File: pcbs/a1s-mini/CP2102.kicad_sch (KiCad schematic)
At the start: 12 parts, among them U3 CP2102N

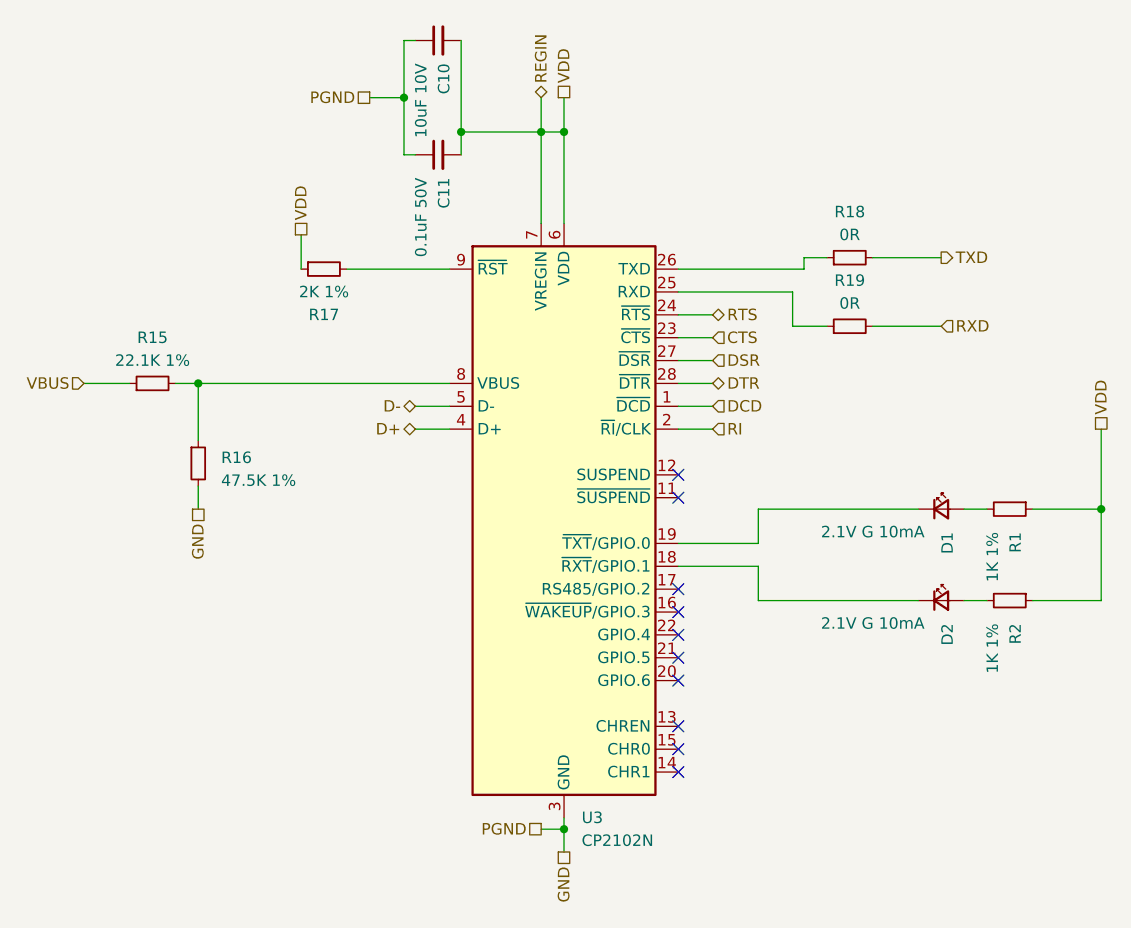
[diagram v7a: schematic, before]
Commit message: Collateral update of A1S mini (TX LEDs fix)
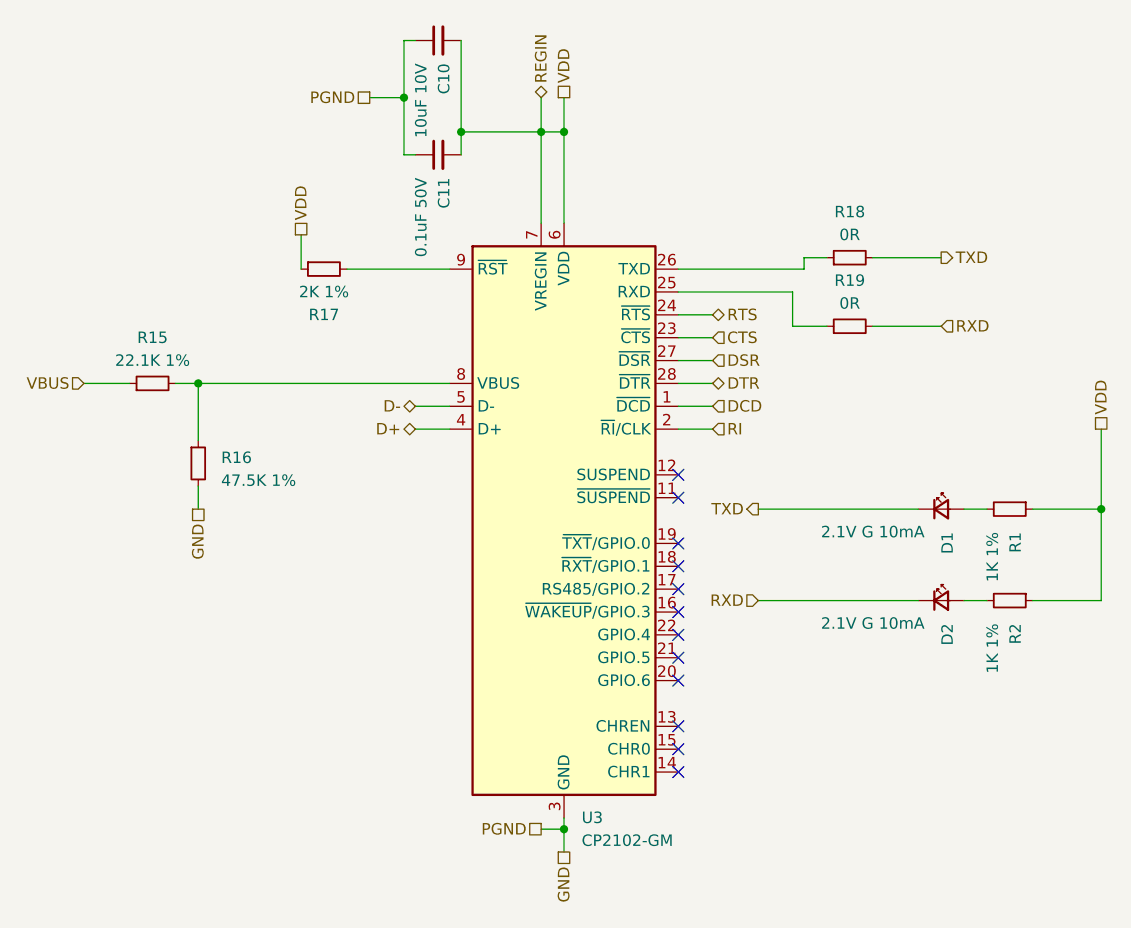
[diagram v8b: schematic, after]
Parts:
- U3: value CP2102N -> CP2102-GM; Manufacturer_Part_Number CP2102N-A02-GQFN28R -> CP2102-GM
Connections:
- net RXD: now also D2.1 (K)
- net TXD: now also D1.1 (K)
- net at U3.18 (~{RXT}/GPIO.1): no longer D2.1 (K)
- net at U3.19 (~{TXT}/GPIO.0): no longer D1.1 (K)
- no-connect marks 10 -> 12
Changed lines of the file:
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@@
 	(title_block
 		(title "A1S Mini Board")
-		(date "2025-03-30")
-		(rev "0.3.0")
+		(date "2025-10-05")
+		(rev "0.3.2")
 		(company "Martin Roger")
 	)
@@
 	)
 	(no_connect
+		(at 166.37 106.68)
+	)
+	(no_connect
 		(at 166.37 127)
 	)
@@
 		(at 166.37 114.3)
 	)
+	(no_connect
+		(at 166.37 104.14)
+	)
 	(wire
 		(pts
@@
 	(wire
 		(pts
-			(xy 175.26 104.14) (xy 166.37 104.14)
-		)
-		(stroke
-			(width 0)
-			(type default)
-		)
-	)
-	(wire
-		(pts
 			(xy 137.16 88.9) (xy 140.97 88.9)
 		)
@@
 	(wire
 		(pts
-			(xy 175.26 110.49) (xy 175.26 106.68)
-		)
-		(stroke
-			(width 0)
-			(type default)
-		)
-	)
-	(wire
-		(pts
-			(xy 175.26 100.33) (xy 175.26 104.14)
-		)
-		(stroke
-			(width 0)
-			(type default)
-		)
-	)
-	(wire
-		(pts
 			(xy 187.96 80.01) (xy 195.58 80.01)
 		)
@@
 		(pts
 			(xy 113.03 86.36) (xy 113.03 92.71)
-		)
-		(stroke
-			(width 0)
-			(type default)
-		)
-	)
-	(wire
-		(pts
-			(xy 175.26 106.68) (xy 166.37 106.68)
 		)
 		(stroke
@@
 		)
 	)
+	(hierarchical_label "RXD"
+		(shape input)
+		(at 175.26 110.49 180)
+		(effects
+			(font
+				(size 1.27 1.27)
+			)
+			(justify right)
+		)
+	)
 	(hierarchical_label "DTR"
 		(shape bidirectional)
@@
 		(shape bidirectional)
 		(at 137.16 91.44 180)
+		(effects
+			(font
+				(size 1.27 1.27)
+			)
+			(justify right)
+		)
+	)
+	(hierarchical_label "TXD"
+		(shape output)
+		(at 175.26 100.33 180)
 		(effects
 			(font
@@
 		(instances
 			(project "a1s-mini"
-				(path "/473bba75-08f8-4c6c-a9b2-aa3e95e63a5e/124ee9d1-939d-44ed-a223-ddb52f42937f"
-					(reference "R34")
-					(unit 1)
-				)
 				(path "/473bba75-08f8-4c6c-a9b2-aa3e95e63a5e/82540054-4b5d-493e-806c-5bb240b603f8"
 					(reference "R1")
@@
 		(instances
 			(project "a1s-mini"
-				(path "/473bba75-08f8-4c6c-a9b2-aa3e95e63a5e/124ee9d1-939d-44ed-a223-ddb52f42937f"
-					(reference "C14")
-					(unit 1)
-				)
 				(path "/473bba75-08f8-4c6c-a9b2-aa3e95e63a5e/82540054-4b5d-493e-806c-5bb240b603f8"
 					(reference "C11")
@@
 		(instances
 			(project "a1s-mini"
-				(path "/473bba75-08f8-4c6c-a9b2-aa3e95e63a5e/124ee9d1-939d-44ed-a223-ddb52f42937f"
-					(reference "D11")
-					(unit 1)
-				)
 				(path "/473bba75-08f8-4c6c-a9b2-aa3e95e63a5e/82540054-4b5d-493e-806c-5bb240b603f8"
 					(reference "D2")
@@
 		(instances
 			(project "a1s-mini"
-				(path "/473bba75-08f8-4c6c-a9b2-aa3e95e63a5e/124ee9d1-939d-44ed-a223-ddb52f42937f"
-					(reference "D9")
-					(unit 1)
-				)
 				(path "/473bba75-08f8-4c6c-a9b2-aa3e95e63a5e/82540054-4b5d-493e-806c-5bb240b603f8"
 					(reference "D1")
@@
 		(instances
 			(project "a1s-mini"
-				(path "/473bba75-08f8-4c6c-a9b2-aa3e95e63a5e/124ee9d1-939d-44ed-a223-ddb52f42937f"
-					(reference "R27")
-					(unit 1)
-				)
 				(path "/473bba75-08f8-4c6c-a9b2-aa3e95e63a5e/82540054-4b5d-493e-806c-5bb240b603f8"
 					(reference "R19")
@@
 		(instances
 			(project "a1s-mini"
-				(path "/473bba75-08f8-4c6c-a9b2-aa3e95e63a5e/124ee9d1-939d-44ed-a223-ddb52f42937f"
-					(reference "C13")
-					(unit 1)
-				)
 				(path "/473bba75-08f8-4c6c-a9b2-aa3e95e63a5e/82540054-4b5d-493e-806c-5bb240b603f8"
 					(reference "C10")
@@
 		(instances
 			(project "a1s-mini"
-				(path "/473bba75-08f8-4c6c-a9b2-aa3e95e63a5e/124ee9d1-939d-44ed-a223-ddb52f42937f"
-					(reference "R23")
-					(unit 1)
-				)
 				(path "/473bba75-08f8-4c6c-a9b2-aa3e95e63a5e/82540054-4b5d-493e-806c-5bb240b603f8"
 					(reference "R15")
@@
 		(instances
 			(project "a1s-mini"
-				(path "/473bba75-08f8-4c6c-a9b2-aa3e95e63a5e/124ee9d1-939d-44ed-a223-ddb52f42937f"
-					(reference "R35")
-					(unit 1)
-				)
 				(path "/473bba75-08f8-4c6c-a9b2-aa3e95e63a5e/82540054-4b5d-493e-806c-5bb240b603f8"
 					(reference "R2")
@@
 		(instances
 			(project "a1s-mini"
-				(path "/473bba75-08f8-4c6c-a9b2-aa3e95e63a5e/124ee9d1-939d-44ed-a223-ddb52f42937f"
-					(reference "R26")
-					(unit 1)
-				)
 				(path "/473bba75-08f8-4c6c-a9b2-aa3e95e63a5e/82540054-4b5d-493e-806c-5bb240b603f8"
 					(reference "R18")
@@
 		(instances
 			(project "a1s-mini"
-				(path "/473bba75-08f8-4c6c-a9b2-aa3e95e63a5e/124ee9d1-939d-44ed-a223-ddb52f42937f"
-					(reference "R25")
-					(unit 1)
-				)
 				(path "/473bba75-08f8-4c6c-a9b2-aa3e95e63a5e/82540054-4b5d-493e-806c-5bb240b603f8"
 					(reference "R17")
@@
 		(instances
 			(project "a1s-mini"
-				(path "/473bba75-08f8-4c6c-a9b2-aa3e95e63a5e/124ee9d1-939d-44ed-a223-ddb52f42937f"
-					(reference "R24")
-					(unit 1)
-				)
 				(path "/473bba75-08f8-4c6c-a9b2-aa3e95e63a5e/82540054-4b5d-493e-806c-5bb240b603f8"
 					(reference "R16")
@@
 			)
 		)
-		(property "Value" "CP2102N"
+		(property "Value" "CP2102-GM"
 			(at 155.6259 137.16 0)
 			(effects
@@
 			)
 		)
-		(property "Datasheet" "https://www.silabs.com/documents/public/data-sheets/cp2102n-datasheet.pdf"
+		(property "Datasheet" "https://www.silabs.com/documents/public/data-sheets/CP2102-9.pdf"
 			(at 154.94 120.65 0)
 			(effects
@@
 			)
 		)
-		(property "Manufacturer_Part_Number" "CP2102N-A02-GQFN28R"
+		(property "Manufacturer_Part_Number" "CP2102-GM"
 			(at 153.67 101.6 0)
 			(effects
@@
 		(instances
 			(project "a1s-mini"
-				(path "/473bba75-08f8-4c6c-a9b2-aa3e95e63a5e/124ee9d1-939d-44ed-a223-ddb52f42937f"
-					(reference "U4")
-					(unit 1)
-				)
 				(path "/473bba75-08f8-4c6c-a9b2-aa3e95e63a5e/82540054-4b5d-493e-806c-5bb240b603f8"
 					(reference "U3")
